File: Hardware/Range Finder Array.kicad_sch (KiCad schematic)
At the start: 24 parts

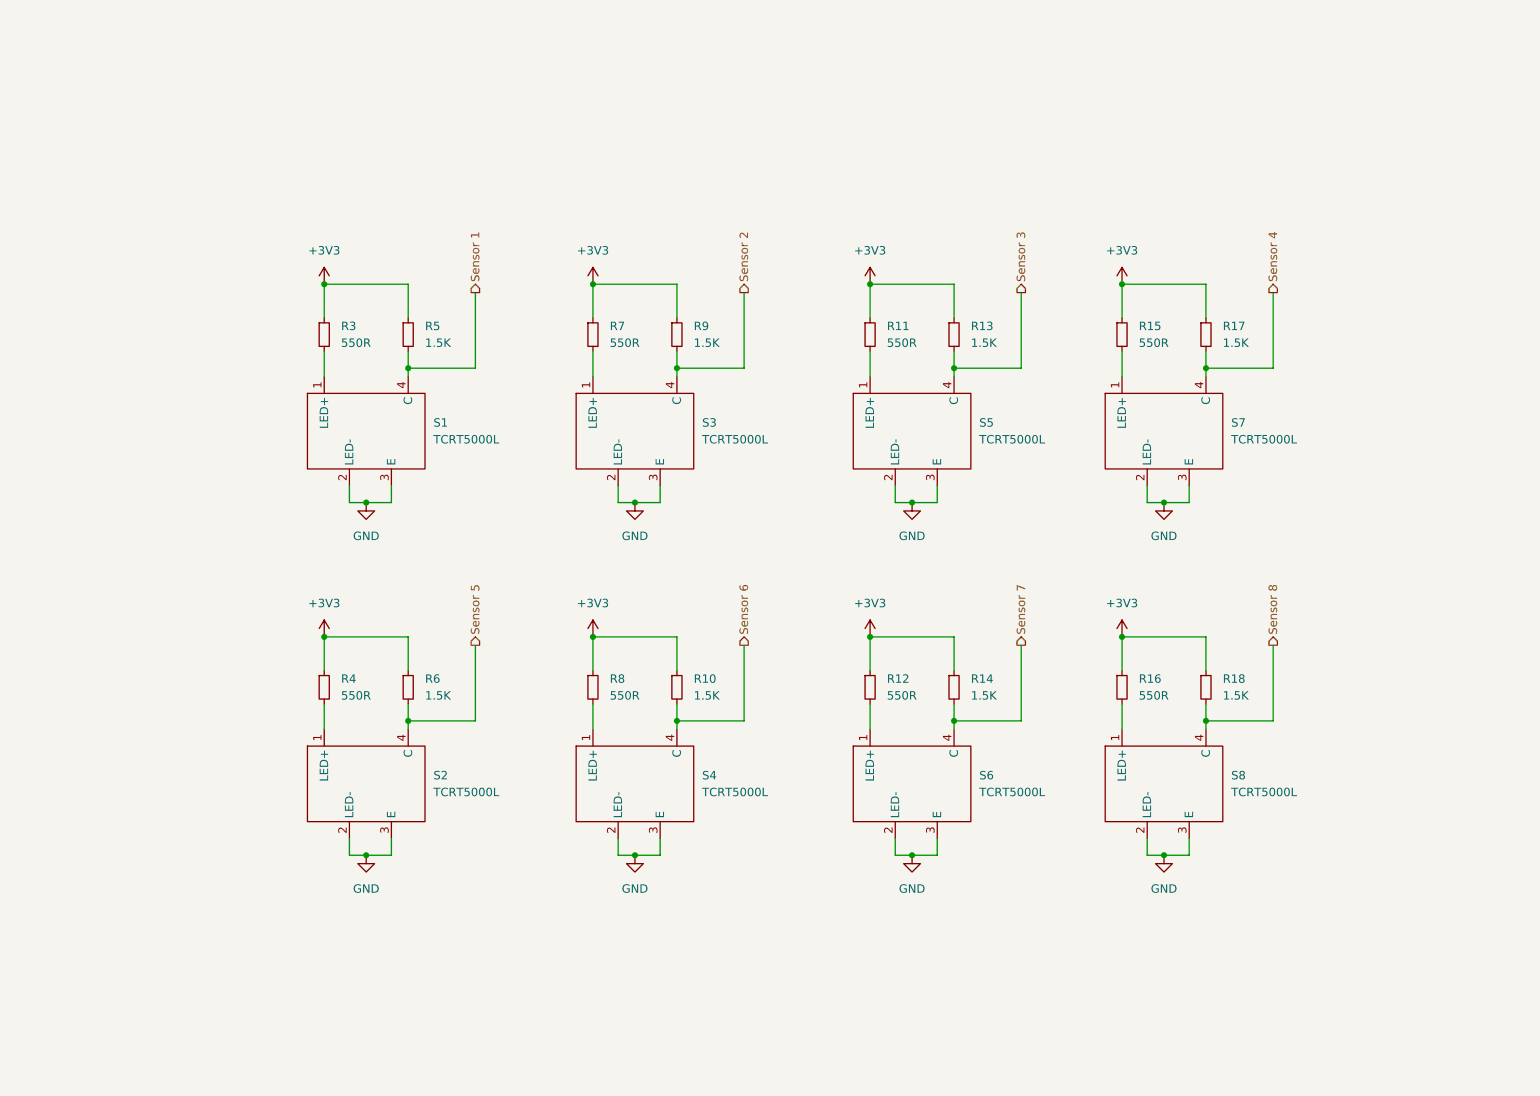
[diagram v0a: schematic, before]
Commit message: Add new array for sensors
Add in sensor array

Begin trace reroute
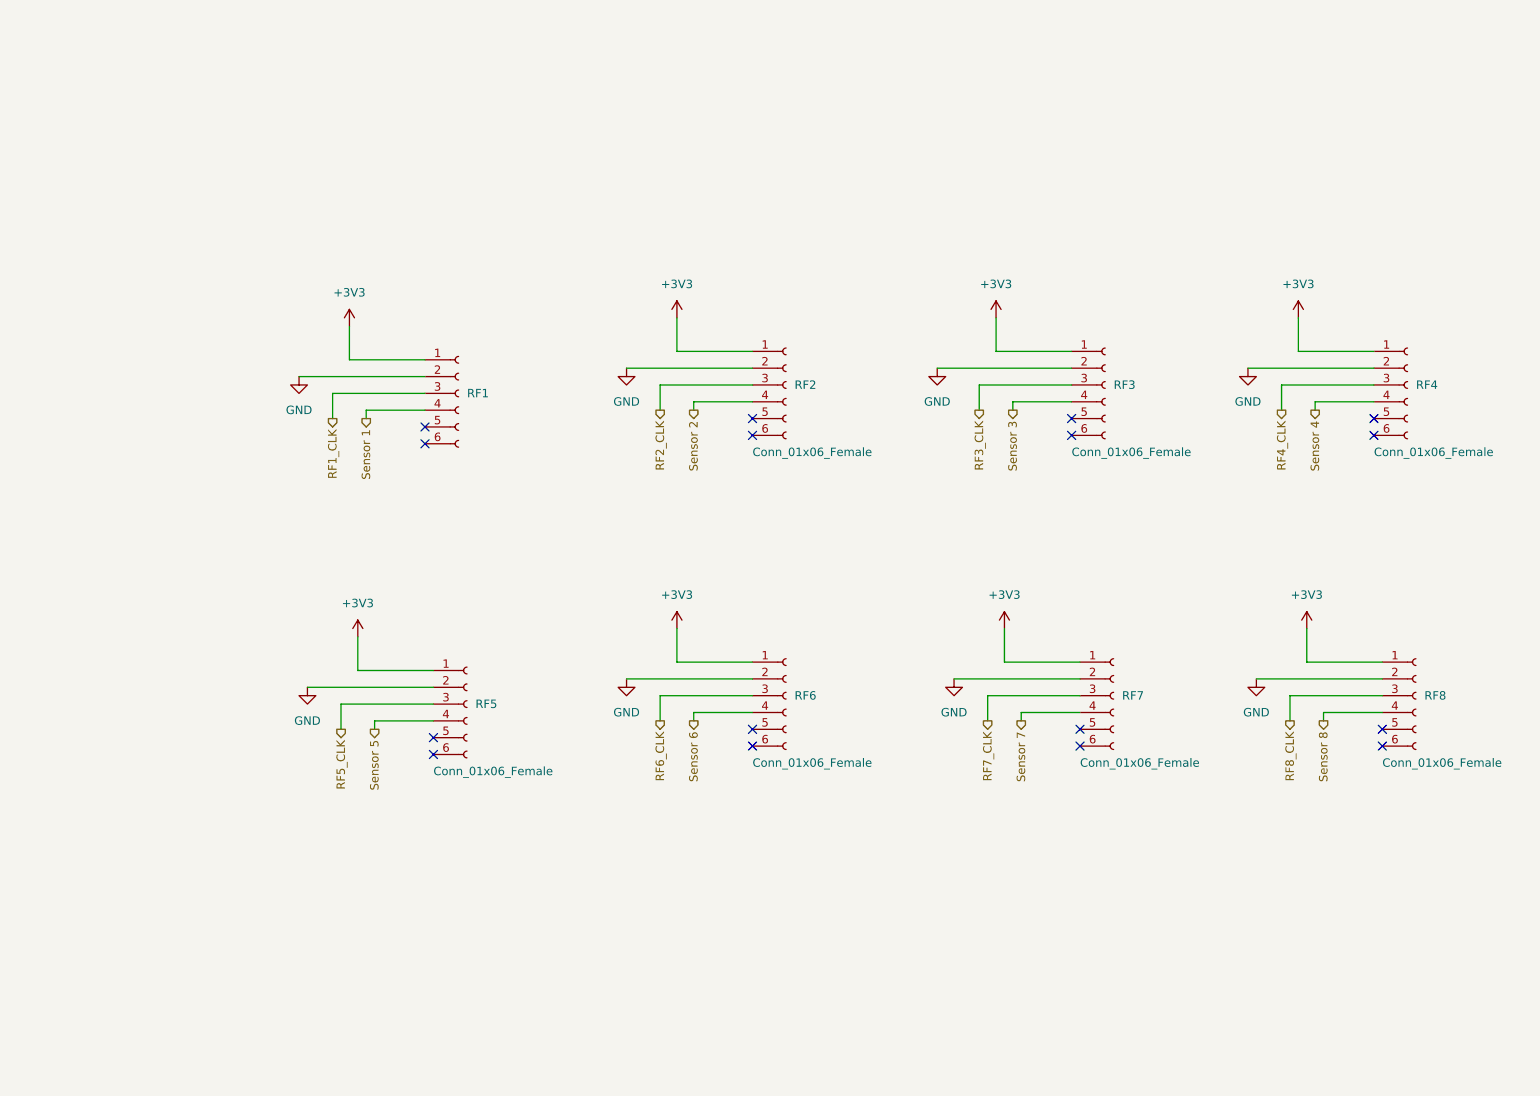
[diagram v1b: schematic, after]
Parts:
- removed R10, R13, R14, R17, R18, R5, R6, R9: 1.5K, Resistor_SMD:R_0805_2012Metric, symbol Device:R_Small
- removed R11, R12, R15, R16, R3, R4, R7, R8: 550R, Resistor_SMD:R_0805_2012Metric, symbol Device:R_Small
- removed S1, S2, S3, S4, S5, S6, S7, S8: TCRT5000L, Amoskeag_KiCAD_Lib:TCRT5000L, symbol Amoskeag-KiCAD-Lib:TCRT5000L
- added RF1: (no value), symbol Connector:Conn_01x06_Female
- added RF2, RF3, RF4, RF5, RF6, RF7, RF8: Conn_01x06_Female, Connector_PinHeader_2.54mm:PinHeader_1x06_P2.54mm_Vertical, symbol Connector:Conn_01x06_Female
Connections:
- net +3V3: now also RF1.1 (Pin_1), RF2.1 (Pin_1), RF3.1 (Pin_1), RF4.1 (Pin_1), RF5.1 (Pin_1), RF6.1 (Pin_1), RF7.1 (Pin_1), RF8.1 (Pin_1)
- net GND: now also RF1.2 (Pin_2), RF2.2 (Pin_2), RF3.2 (Pin_2), RF4.2 (Pin_2), RF5.2 (Pin_2), RF6.2 (Pin_2), RF7.2 (Pin_2), RF8.2 (Pin_2)
- net Sensor 1: now also RF1.4 (Pin_4)
- net Sensor 2: now also RF2.4 (Pin_4)
- net Sensor 3: now also RF3.4 (Pin_4)
- net Sensor 4: now also RF4.4 (Pin_4)
- net Sensor 5: now also RF5.4 (Pin_4)
- net Sensor 6: now also RF6.4 (Pin_4)
- net Sensor 7: now also RF7.4 (Pin_4)
- net Sensor 8: now also RF8.4 (Pin_4)
- new net RF1_CLK: RF1.3 (Pin_3)
- new net RF2_CLK: RF2.3 (Pin_3)
- new net RF3_CLK: RF3.3 (Pin_3)
- new net RF4_CLK: RF4.3 (Pin_3)
- new net RF5_CLK: RF5.3 (Pin_3)
- new net RF6_CLK: RF6.3 (Pin_3)
- new net RF7_CLK: RF7.3 (Pin_3)
- new net RF8_CLK: RF8.3 (Pin_3)
- no-connect marks 0 -> 16

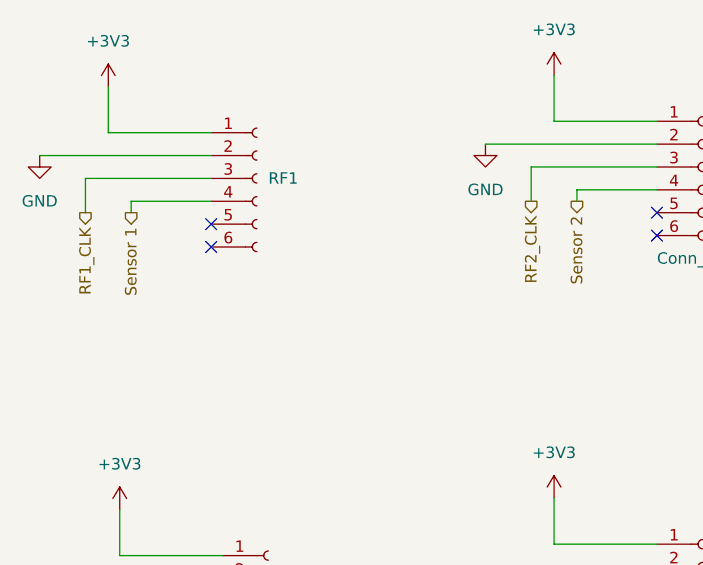
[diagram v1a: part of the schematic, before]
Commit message: I2C Interface Established
Run Traces for all Sensors

Mark unused Pins

Sub-Optimally run said traces
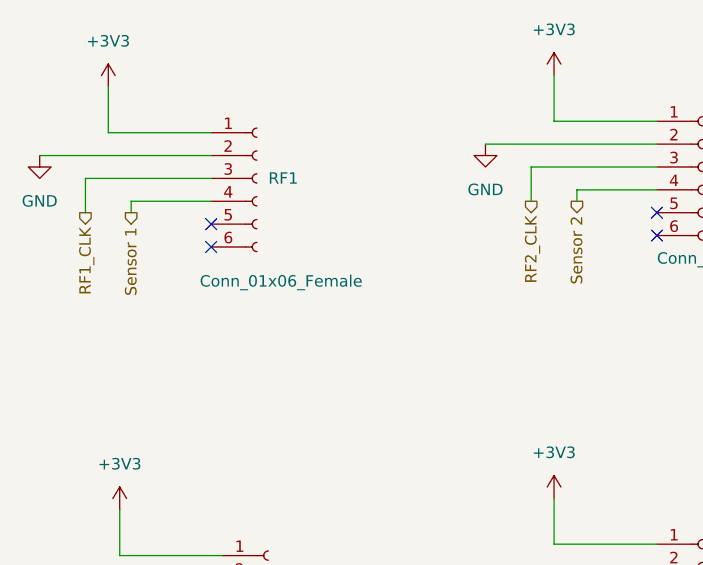
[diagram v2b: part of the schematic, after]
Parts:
- RF1: value (none) -> Conn_01x06_Female; footprint (none) -> Connector_PinHeader_2.54mm:PinHeader_1x06_P2.54mm_Vertical
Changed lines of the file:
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@@
       (effects (font (size 1.27 1.27)) (justify left))
     )
-    (property "Value" "" (id 1) (at 83.82 93.98 0)
+    (property "Value" "Conn_01x06_Female" (id 1) (at 83.82 93.98 0)
       (effects (font (size 1.27 1.27)) (justify left))
     )
-    (property "Footprint" "" (id 2) (at 90.17 82.55 0)
+    (property "Footprint" "Connector_PinHeader_2.54mm:PinHeader_1x06_P2.54mm_Vertical" (id 2) (at 90.17 82.55 0)
       (effects (font (size 1.27 1.27)) hide)
     )

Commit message: Fix Traces
trace fixes
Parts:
- renumbered RF5 to RF2, RF2 to RF3, RF6 to RF4, RF3 to RF5, RF7 to RF6, RF4 to RF7
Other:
- company: (none) -> Amoskeag Technologies
- title: (none) -> TurtleBot Mainboard
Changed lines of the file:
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@@
 (kicad_sch (version 20211123) (generator eeschema)
   (paper "A4")
+  (title_block
+    (title "TurtleBot Mainboard")
+    (date "2022-11-27")
+    (rev "${REVISION}")
+    (company "Amoskeag Technologies")
+    (comment 4 "${FULL_REVISION}")
+  )
   (no_connect (at 184.15 133.35))
   (no_connect (at 182.88 88.9))
@@
   (symbol (lib_id "Connector:Conn_01x06_Female") (at 189.23 128.27 0) (unit 1)
     (in_bom yes) (on_board yes)
-    (property "Reference" "RF7" (id 0) (at 190.5 128.2699 0)
+    (property "Reference" "RF6" (id 0) (at 190.5 128.2699 0)
       (effects (font (size 1.27 1.27)) (justify left))
     )
@@
   (symbol (lib_id "power:+3V3") (at 74.93 119.38 0) (unit 1)
     (in_bom yes) (on_board yes)
-    (property "Reference" "#PWR0111" (id 0) (at 74.93 123.19 0)
+    (property "Reference" "#PWR038" (id 0) (at 74.93 123.19 0)
       (effects (font (size 1.27 1.27)) hide)
     )
@@
   (symbol (lib_id "Connector:Conn_01x06_Female") (at 91.44 129.54 0) (unit 1)
     (in_bom yes) (on_board yes)
-    (property "Reference" "RF5" (id 0) (at 92.71 129.5399 0)
+    (property "Reference" "RF2" (id 0) (at 92.71 129.5399 0)
       (effects (font (size 1.27 1.27)) (justify left))
     )
@@
   (symbol (lib_id "power:GND") (at 165.1 125.73 0) (unit 1)
     (in_bom yes) (on_board yes) (fields_autoplaced)
-    (property "Reference" "#PWR0116" (id 0) (at 165.1 132.08 0)
+    (property "Reference" "#PWR044" (id 0) (at 165.1 132.08 0)
       (effects (font (size 1.27 1.27)) hide)
     )
@@
   (symbol (lib_id "Connector:Conn_01x06_Female") (at 139.7 128.27 0) (unit 1)
     (in_bom yes) (on_board yes)
-    (property "Reference" "RF6" (id 0) (at 140.97 128.2699 0)
+    (property "Reference" "RF4" (id 0) (at 140.97 128.2699 0)
       (effects (font (size 1.27 1.27)) (justify left))
     )
@@
   (symbol (lib_id "power:+3V3") (at 172.72 118.11 0) (unit 1)
     (in_bom yes) (on_board yes)
-    (property "Reference" "#PWR0115" (id 0) (at 172.72 121.92 0)
+    (property "Reference" "#PWR046" (id 0) (at 172.72 121.92 0)
       (effects (font (size 1.27 1.27)) hide)
     )
@@
   (symbol (lib_id "Connector:Conn_01x06_Female") (at 139.7 81.28 0) (unit 1)
     (in_bom yes) (on_board yes)
-    (property "Reference" "RF2" (id 0) (at 140.97 81.2799 0)
+    (property "Reference" "RF3" (id 0) (at 140.97 81.2799 0)
       (effects (font (size 1.27 1.27)) (justify left))
     )
@@
   (symbol (lib_id "power:GND") (at 115.57 78.74 0) (unit 1)
     (in_bom yes) (on_board yes) (fields_autoplaced)
-    (property "Reference" "#PWR0113" (id 0) (at 115.57 85.09 0)
+    (property "Reference" "#PWR039" (id 0) (at 115.57 85.09 0)
       (effects (font (size 1.27 1.27)) hide)
     )
@@
   (symbol (lib_id "power:+3V3") (at 171.45 71.12 0) (unit 1)
     (in_bom yes) (on_board yes)
-    (property "Reference" "#PWR0108" (id 0) (at 171.45 74.93 0)
+    (property "Reference" "#PWR045" (id 0) (at 171.45 74.93 0)
       (effects (font (size 1.27 1.27)) hide)
     )
@@
   (symbol (lib_id "power:GND") (at 210.82 125.73 0) (unit 1)
     (in_bom yes) (on_board yes) (fields_autoplaced)
-    (property "Reference" "#PWR0103" (id 0) (at 210.82 132.08 0)
+    (property "Reference" "#PWR048" (id 0) (at 210.82 132.08 0)
       (effects (font (size 1.27 1.27)) hide)
     )
@@
   (symbol (lib_id "power:+3V3") (at 73.66 72.39 0) (unit 1)
     (in_bom yes) (on_board yes)
-    (property "Reference" "#PWR0101" (id 0) (at 73.66 76.2 0)
+    (property "Reference" "#PWR037" (id 0) (at 73.66 76.2 0)
       (effects (font (size 1.27 1.27)) hide)
     )
@@
   (symbol (lib_id "power:+3V3") (at 123.19 118.11 0) (unit 1)
     (in_bom yes) (on_board yes)
-    (property "Reference" "#PWR0114" (id 0) (at 123.19 121.92 0)
+    (property "Reference" "#PWR042" (id 0) (at 123.19 121.92 0)
       (effects (font (size 1.27 1.27)) hide)
     )
@@
   (symbol (lib_id "power:+3V3") (at 217.17 71.12 0) (unit 1)
     (in_bom yes) (on_board yes)
-    (property "Reference" "#PWR0106" (id 0) (at 217.17 74.93 0)
+    (property "Reference" "#PWR049" (id 0) (at 217.17 74.93 0)
       (effects (font (size 1.27 1.27)) hide)
     )
@@
   (symbol (lib_id "power:GND") (at 162.56 78.74 0) (unit 1)
     (in_bom yes) (on_board yes) (fields_autoplaced)
-    (property "Reference" "#PWR0107" (id 0) (at 162.56 85.09 0)
+    (property "Reference" "#PWR043" (id 0) (at 162.56 85.09 0)
       (effects (font (size 1.27 1.27)) hide)
     )
@@
   (symbol (lib_id "power:GND") (at 209.55 78.74 0) (unit 1)
     (in_bom yes) (on_board yes) (fields_autoplaced)
-    (property "Reference" "#PWR0105" (id 0) (at 209.55 85.09 0)
+    (property "Reference" "#PWR047" (id 0) (at 209.55 85.09 0)
       (effects (font (size 1.27 1.27)) hide)
     )
@@
   (symbol (lib_id "power:GND") (at 115.57 125.73 0) (unit 1)
     (in_bom yes) (on_board yes) (fields_autoplaced)
-    (property "Reference" "#PWR0112" (id 0) (at 115.57 132.08 0)
+    (property "Reference" "#PWR040" (id 0) (at 115.57 132.08 0)
       (effects (font (size 1.27 1.27)) hide)
     )
@@
   (symbol (lib_id "Connector:Conn_01x06_Female") (at 187.96 81.28 0) (unit 1)
     (in_bom yes) (on_board yes)
-    (property "Reference" "RF3" (id 0) (at 189.23 81.2799 0)
+    (property "Reference" "RF5" (id 0) (at 189.23 81.2799 0)
       (effects (font (size 1.27 1.27)) (justify left))
     )
@@
   (symbol (lib_id "power:GND") (at 67.31 127 0) (unit 1)
     (in_bom yes) (on_board yes) (fields_autoplaced)
-    (property "Reference" "#PWR0110" (id 0) (at 67.31 133.35 0)
+    (property "Reference" "#PWR036" (id 0) (at 67.31 133.35 0)
       (effects (font (size 1.27 1.27)) hide)
     )
@@
   (symbol (lib_id "power:+3V3") (at 123.19 71.12 0) (unit 1)
     (in_bom yes) (on_board yes)
-    (property "Reference" "#PWR0109" (id 0) (at 123.19 74.93 0)
+    (property "Reference" "#PWR041" (id 0) (at 123.19 74.93 0)
       (effects (font (size 1.27 1.27)) hide)
     )
@@
   (symbol (lib_id "power:GND") (at 66.04 80.01 0) (unit 1)
     (in_bom yes) (on_board yes) (fields_autoplaced)
-    (property "Reference" "#PWR0102" (id 0) (at 66.04 86.36 0)
+    (property "Reference" "#PWR035" (id 0) (at 66.04 86.36 0)
       (effects (font (size 1.27 1.27)) hide)
     )
@@
   (symbol (lib_id "Connector:Conn_01x06_Female") (at 233.68 81.28 0) (unit 1)
     (in_bom yes) (on_board yes)
-    (property "Reference" "RF4" (id 0) (at 234.95 81.2799 0)
+    (property "Reference" "RF7" (id 0) (at 234.95 81.2799 0)
       (effects (font (size 1.27 1.27)) (justify left))
     )
@@
   (symbol (lib_id "power:+3V3") (at 218.44 118.11 0) (unit 1)
     (in_bom yes) (on_board yes)
-    (property "Reference" "#PWR0104" (id 0) (at 218.44 121.92 0)
-      (effects (font (size 1.27 1.27)) hide)
-    )
+    (property "Reference" "#PWR050" (id 0) (at 218.44 121.92 0)
+      (effects (font (size 1.27 1.27)) hide)
+    )
